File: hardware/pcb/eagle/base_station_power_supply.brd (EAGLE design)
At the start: 30 x 68.5 mm, 17 parts, among them CON1 POWER_JACKPTH, IC1 MB16S-TP

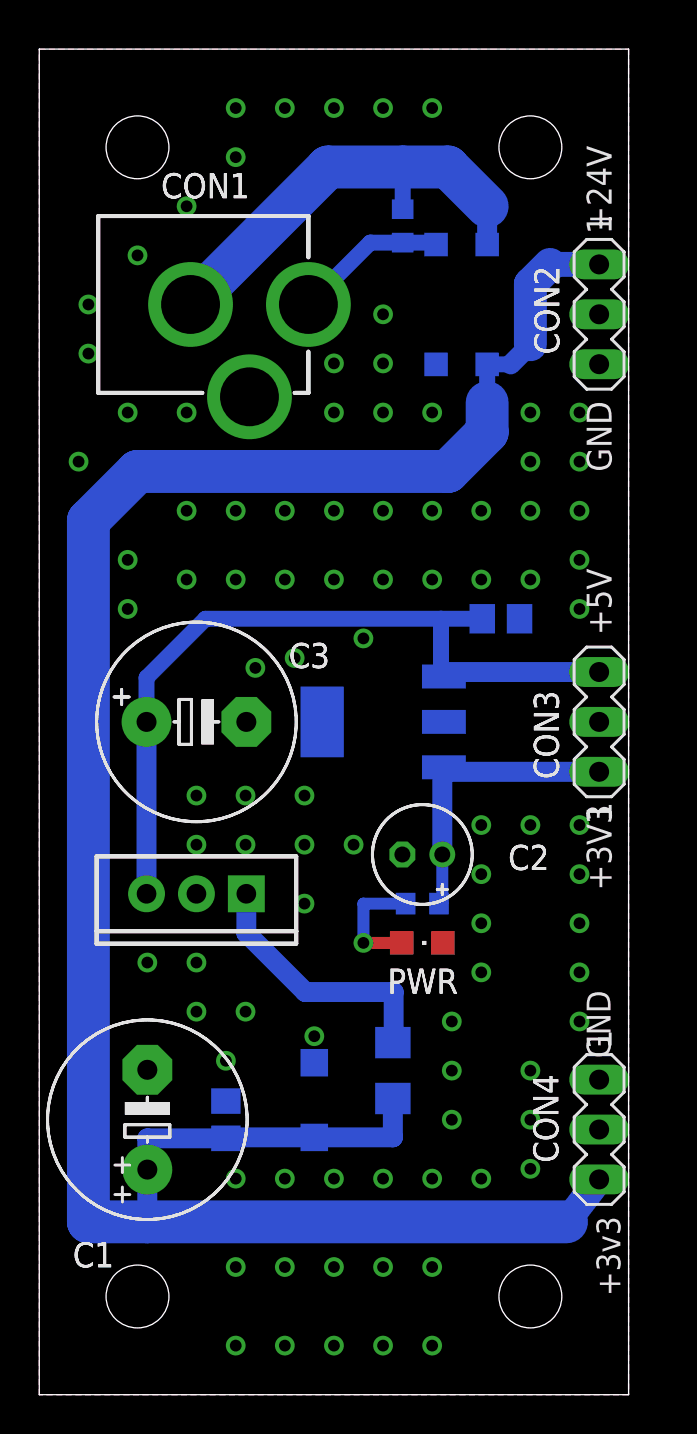
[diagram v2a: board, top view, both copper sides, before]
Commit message: Silk screen layer tidied up
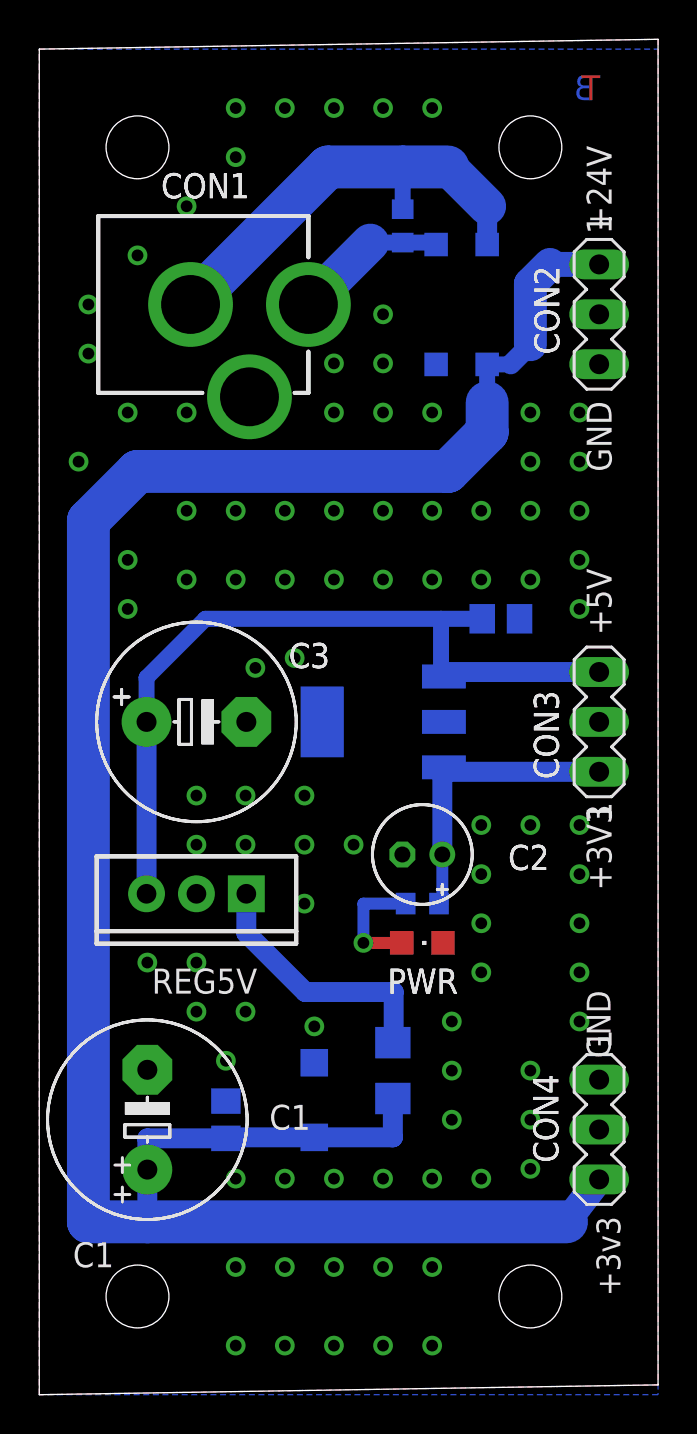
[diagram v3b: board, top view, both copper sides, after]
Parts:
- removed D1A: PESD0603-240, texas_lvds:D0603
- added D2: SMF24A, texas_lvds:SOD123
- D1: value SMF24A -> PESD0603-240; device texas_lvds:SOD123 -> texas_lvds:D0603
- moved D1 44.7 mm to (18.5, 59.5), turned to 270 degrees
- renumbered R28 to R1
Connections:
- net +24V: now also D2.C; no longer D1.C
- net GNDINT: now also D2.A; no longer D1.A
- net N$7: now also D1.2; no longer D1A.2
- net N$8: now also D1.1; no longer D1A.1
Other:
- board size 30 x 68.5 mm -> 31.5 x 69 mm
- board text added: "B"
- board text added: "D2"
- board text added: "R1"
- board text added: "REG5V"
- board text added: "T"
- board text removed: "D1A"
- board text removed: "R28"
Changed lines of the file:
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@@
 <hole x="5" y="63.5" drill="3.2"/>
 <hole x="5" y="5" drill="3.2"/>
-<wire x1="30" y1="0" x2="0" y2="0" width="0" layer="20"/>
+<wire x1="31.5" y1="0.5" x2="0" y2="0" width="0" layer="20"/>
 <wire x1="0" y1="68.5" x2="0" y2="0" width="0" layer="20"/>
 <hole x="25" y="63.5" drill="3.2"/>
-<wire x1="30" y1="68.5" x2="30" y2="0" width="0" layer="20"/>
-<wire x1="30" y1="68.5" x2="0" y2="68.5" width="0" layer="20"/>
+<wire x1="31.5" y1="69" x2="31.5" y2="0.5" width="0" layer="20"/>
+<wire x1="31.5" y1="69" x2="0" y2="68.5" width="0" layer="20"/>
 <wire x1="5.499996875" y1="12.857003125" x2="5.499996875" y2="13.111003125" width="0.1524" layer="121"/>
 <wire x1="5.499996875" y1="13.111003125" x2="6.642996875" y2="13.111003125" width="0.1524" layer="121"/>
@@
 <circle x="5.499996875" y="14.000003125" radius="5.08" width="0.1524" layer="121"/>
 <rectangle x1="5.182496875" y1="13.428503125" x2="5.817496875" y2="15.714503125" layer="121" rot="R90"/>
-<text x="3.80099375" y="7.7568125" size="1.27" layer="121" font="vector" ratio="10" rot="R180">C1</text>
+<text x="13.80099375" y="14.7568125" size="1.27" layer="121" font="vector" ratio="10" rot="R180">C1</text>
 <wire x1="20.769996875" y1="25.72200625" x2="20.261996875" y2="25.72200625" width="0.1524" layer="121"/>
 <wire x1="20.515996875" y1="25.97600625" x2="20.515996875" y2="25.46800625" width="0.1524" layer="121"/>
@@
 <text x="27.865003125" y="20.580009375" size="1.217" layer="121" font="vector" ratio="10" rot="R270">GND</text>
 <text x="25.1509875" y="16.310009375" size="1.27" layer="121" font="vector" ratio="10" rot="R270">CON4</text>
-<text x="13.40000625" y="9.699990625" size="1.27" layer="122" font="vector" ratio="10" rot="MR90">D1</text>
-<text x="17.615009375" y="62.765009375" size="1.27" layer="122" font="vector" ratio="10" rot="MR180">D1A</text>
+<text x="13.40000625" y="9.699990625" size="1.27" layer="122" font="vector" ratio="10" rot="MR90">D2</text>
+<text x="17.615009375" y="62.765009375" size="1.27" layer="122" font="vector" ratio="10" rot="MR180">D1</text>
 <text x="21.007003125" y="17.497003125" size="1.27" layer="122" font="vector" ratio="10" rot="MR270">F1</text>
 <wire x1="19.150009375" y1="53.500003125" x2="23.85" y2="53.500003125" width="0.2032" layer="122"/>
@@
 <rectangle x1="19.5" y1="22.899990625" x2="19.69999375" y2="23.099990625" layer="121" rot="R270"/>
 <text x="17.729996875" y="20.420009375" size="1.27" layer="121" font="vector" ratio="10">PWR</text>
-<text x="21.915003125" y="25.63000625" size="1.27" layer="122" font="vector" ratio="10" rot="MR180">R28</text>
+<text x="21.915003125" y="25.63000625" size="1.27" layer="122" font="vector" ratio="10" rot="MR180">R1</text>
 <wire x1="15.722" y1="30.97340625" x2="19.278" y2="30.97340625" width="0.2032" layer="122"/>
 <wire x1="19.278" y1="30.97340625" x2="19.278" y2="37.52660625" width="0.2032" layer="122"/>
@@
 <text x="27.865003125" y="63.580003125" size="1.27" layer="51" font="vector" ratio="10" rot="R270">+24V</text>
 <text x="27.865003125" y="50.580003125" size="1.27" layer="121" font="vector" ratio="10" rot="R270">GND</text>
+<text x="27.6" y="65.9" size="1.27" layer="1" font="vector" ratio="10">T</text>
+<text x="28.3" y="65.9" size="1.27" layer="16" font="vector" ratio="10" rot="MR0">B</text>
+<text x="5.729996875" y="20.420009375" size="1.27" layer="121" font="vector" ratio="10">REG5V</text>
 </plain>
 <attributes>
@@
 <attribute name="VALUE" x="25.31" y="57.405" size="1.27" layer="28" rot="MR270"/>
 </element>
-<element name="D1" library="texas_lvds" package="SOD123" value="SMF24A" x="14" y="15" smashed="yes" rot="MR90">
+<element name="D2" library="texas_lvds" package="SOD123" value="SMF24A" x="14" y="15" smashed="yes" rot="MR90">
 <attribute name="NAME" x="13.4" y="9.7" size="1.27" layer="26" font="vector" rot="MR90"/>
 <attribute name="VALUE" x="11.7" y="13.9" size="1.27" layer="28" rot="MR90"/>
 </element>
-<element name="D1A" library="texas_lvds" package="D0603" value="PESD0603-240" x="18.5" y="59.5" smashed="yes" rot="MR270">
+<element name="D1" library="texas_lvds" package="D0603" value="PESD0603-240" x="18.5" y="59.5" smashed="yes" rot="MR270">
 <attribute name="NAME" x="17.615" y="62.765" size="1.27" layer="26" font="vector" rot="MR180"/>
 <attribute name="VALUE" x="20.405" y="60.135" size="1.27" layer="28" rot="MR270"/>
@@
 <attribute name="VALUE" x="18.23" y="20.46" size="1.27" layer="27"/>
 </element>
-<element name="R28" library="rcl" package="R0603" value="1k" x="19.5" y="25" smashed="yes" rot="MR180">
+<element name="R1" library="rcl" package="R0603" value="1k" x="19.5" y="25" smashed="yes" rot="MR180">
 <attribute name="NAME" x="21.915" y="25.63" size="1.27" layer="26" font="vector" rot="MR180"/>
 <attribute name="VALUE" x="18.865" y="27.54" size="1.27" layer="28" rot="MR180"/>
@@
 <contactref element="REG3V3" pad="3"/>
 <contactref element="C2" pad="+"/>
-<contactref element="R28" pad="2"/>
+<contactref element="R1" pad="2"/>
 <contactref element="CON3" pad="1"/>
 <wire x1="28.5" y1="31.71" x2="20.5988" y2="31.71" width="1.016" layer="16"/>
@@
 <wire x1="2.5" y1="8.8" x2="5.5" y2="8.8" width="2.1844" layer="16"/>
 <contactref element="IC1" pad="+"/>
-<contactref element="D1" pad="C"/>
+<contactref element="D2" pad="C"/>
 <contactref element="C4" pad="1"/>
 <contactref element="C1" pad="+"/>
@@
 <signal name="GNDINT">
 <polygon width="0.254" layer="16" isolate="0.254">
-<vertex x="30" y="68.5"/>
-<vertex x="30" y="0"/>
+<vertex x="31.5" y="68.5"/>
+<vertex x="31.5" y="0"/>
 <vertex x="0" y="0"/>
 <vertex x="0" y="68.5"/>
 </polygon>
 <polygon width="0.254" layer="1" isolate="0.254" rank="2">
-<vertex x="30" y="68.5"/>
-<vertex x="30" y="0"/>
+<vertex x="31.5" y="69"/>
+<vertex x="31.5" y="0.5"/>
 <vertex x="0" y="0"/>
 <vertex x="0" y="68.5"/>
 </polygon>
 <via x="9.5" y="17" extent="1-16" drill="0.6"/>
-<via x="16.5" y="38.5" extent="1-16" drill="0.6"/>
 <via x="11" y="37" extent="1-16" drill="0.6"/>
-<via x="14" y="18.25" extent="1-16" drill="0.6"/>
+<via x="14" y="18.75" extent="1-16" drill="0.6"/>
 <via x="13" y="37.5" extent="1-16" drill="0.6"/>
 <contactref element="IC1" pad="-"/>
-<contactref element="D1" pad="A"/>
+<contactref element="D2" pad="A"/>
 <contactref element="C4" pad="2"/>
 <contactref element="C1" pad="-"/>
@@
 <contactref element="CON1" pad="PWR"/>
 <contactref element="IC1" pad="~1"/>
-<contactref element="D1A" pad="2"/>
-<wire x1="13.7" y1="55.5" x2="16.85" y2="58.65" width="0.8128" layer="16"/>
+<contactref element="D1" pad="2"/>
+<wire x1="13.7" y1="55.5" x2="16.85" y2="58.65" width="1.9304" layer="16"/>
 <wire x1="16.85" y1="58.65" x2="18.5" y2="58.65" width="0.8128" layer="16"/>
 <wire x1="18.5" y1="58.65" x2="20.2" y2="58.65" width="0.8128" layer="16"/>
@@
 <contactref element="IC1" pad="~2"/>
 <contactref element="CON1" pad="GND"/>
-<contactref element="D1A" pad="1"/>
+<contactref element="D1" pad="1"/>
 <wire x1="18.5" y1="60.35" x2="18.5" y2="62.5" width="0.8128" layer="16"/>
 <wire x1="18.5" y1="62.5" x2="14.7" y2="62.5" width="2.1844" layer="16"/>
 <wire x1="14.7" y1="62.5" x2="7.7" y2="55.5" width="2.1844" layer="16"/>
 <wire x1="22.8" y1="58.55" x2="22.8" y2="60.5" width="1.016" layer="16"/>
-<wire x1="22.8" y1="60.5" x2="20.8" y2="62.5" width="2.1844" layer="16"/>
+<wire x1="22.8" y1="60.5" x2="20.8" y2="62.5" width="1.9304" layer="16"/>
 <wire x1="20.8" y1="62.5" x2="18.5" y2="62.5" width="2.1844" layer="16"/>
 </signal>
 <signal name="N$2">
-<contactref element="R28" pad="1"/>
+<contactref element="R1" pad="1"/>
 <contactref element="PWR" pad="A"/>
 <wire x1="18.45" y1="23" x2="16.5" y2="23" width="0.6096" layer="1"/>
@@
 </signal>
 </signals>
+<errors>
+</errors>
 </board>
 </drawing>

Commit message: Fixed board outline that was accidentally moved
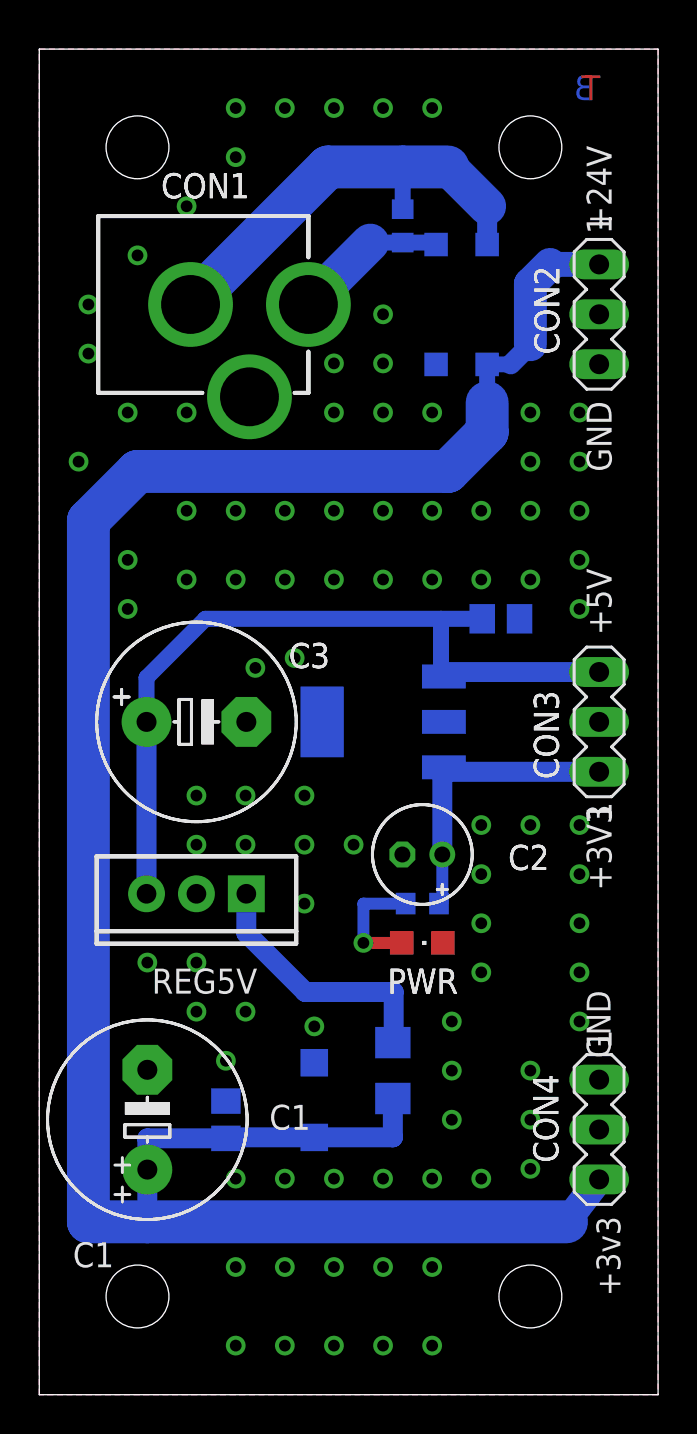
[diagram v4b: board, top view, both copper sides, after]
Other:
- board size 31.5 x 69 mm -> 31.5 x 68.5 mm
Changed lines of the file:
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@@
 <hole x="5" y="63.5" drill="3.2"/>
 <hole x="5" y="5" drill="3.2"/>
-<wire x1="31.5" y1="0.5" x2="0" y2="0" width="0" layer="20"/>
+<wire x1="31.5" y1="0" x2="0" y2="0" width="0" layer="20"/>
 <wire x1="0" y1="68.5" x2="0" y2="0" width="0" layer="20"/>
 <hole x="25" y="63.5" drill="3.2"/>
-<wire x1="31.5" y1="69" x2="31.5" y2="0.5" width="0" layer="20"/>
-<wire x1="31.5" y1="69" x2="0" y2="68.5" width="0" layer="20"/>
+<wire x1="31.5" y1="68.5" x2="31.5" y2="0" width="0" layer="20"/>
+<wire x1="31.5" y1="68.5" x2="0" y2="68.5" width="0" layer="20"/>
 <wire x1="5.499996875" y1="12.857003125" x2="5.499996875" y2="13.111003125" width="0.1524" layer="121"/>
 <wire x1="5.499996875" y1="13.111003125" x2="6.642996875" y2="13.111003125" width="0.1524" layer="121"/>
@@
 </polygon>
 <polygon width="0.254" layer="1" isolate="0.254" rank="2">
-<vertex x="31.5" y="69"/>
-<vertex x="31.5" y="0.5"/>
+<vertex x="31.5" y="68.5"/>
+<vertex x="31.5" y="0"/>
 <vertex x="0" y="0"/>
 <vertex x="0" y="68.5"/>
